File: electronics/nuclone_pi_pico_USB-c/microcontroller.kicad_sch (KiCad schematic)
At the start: 3 parts, among them J5 Conn_02x06_Odd_Even, U3 RaspberryPiPico

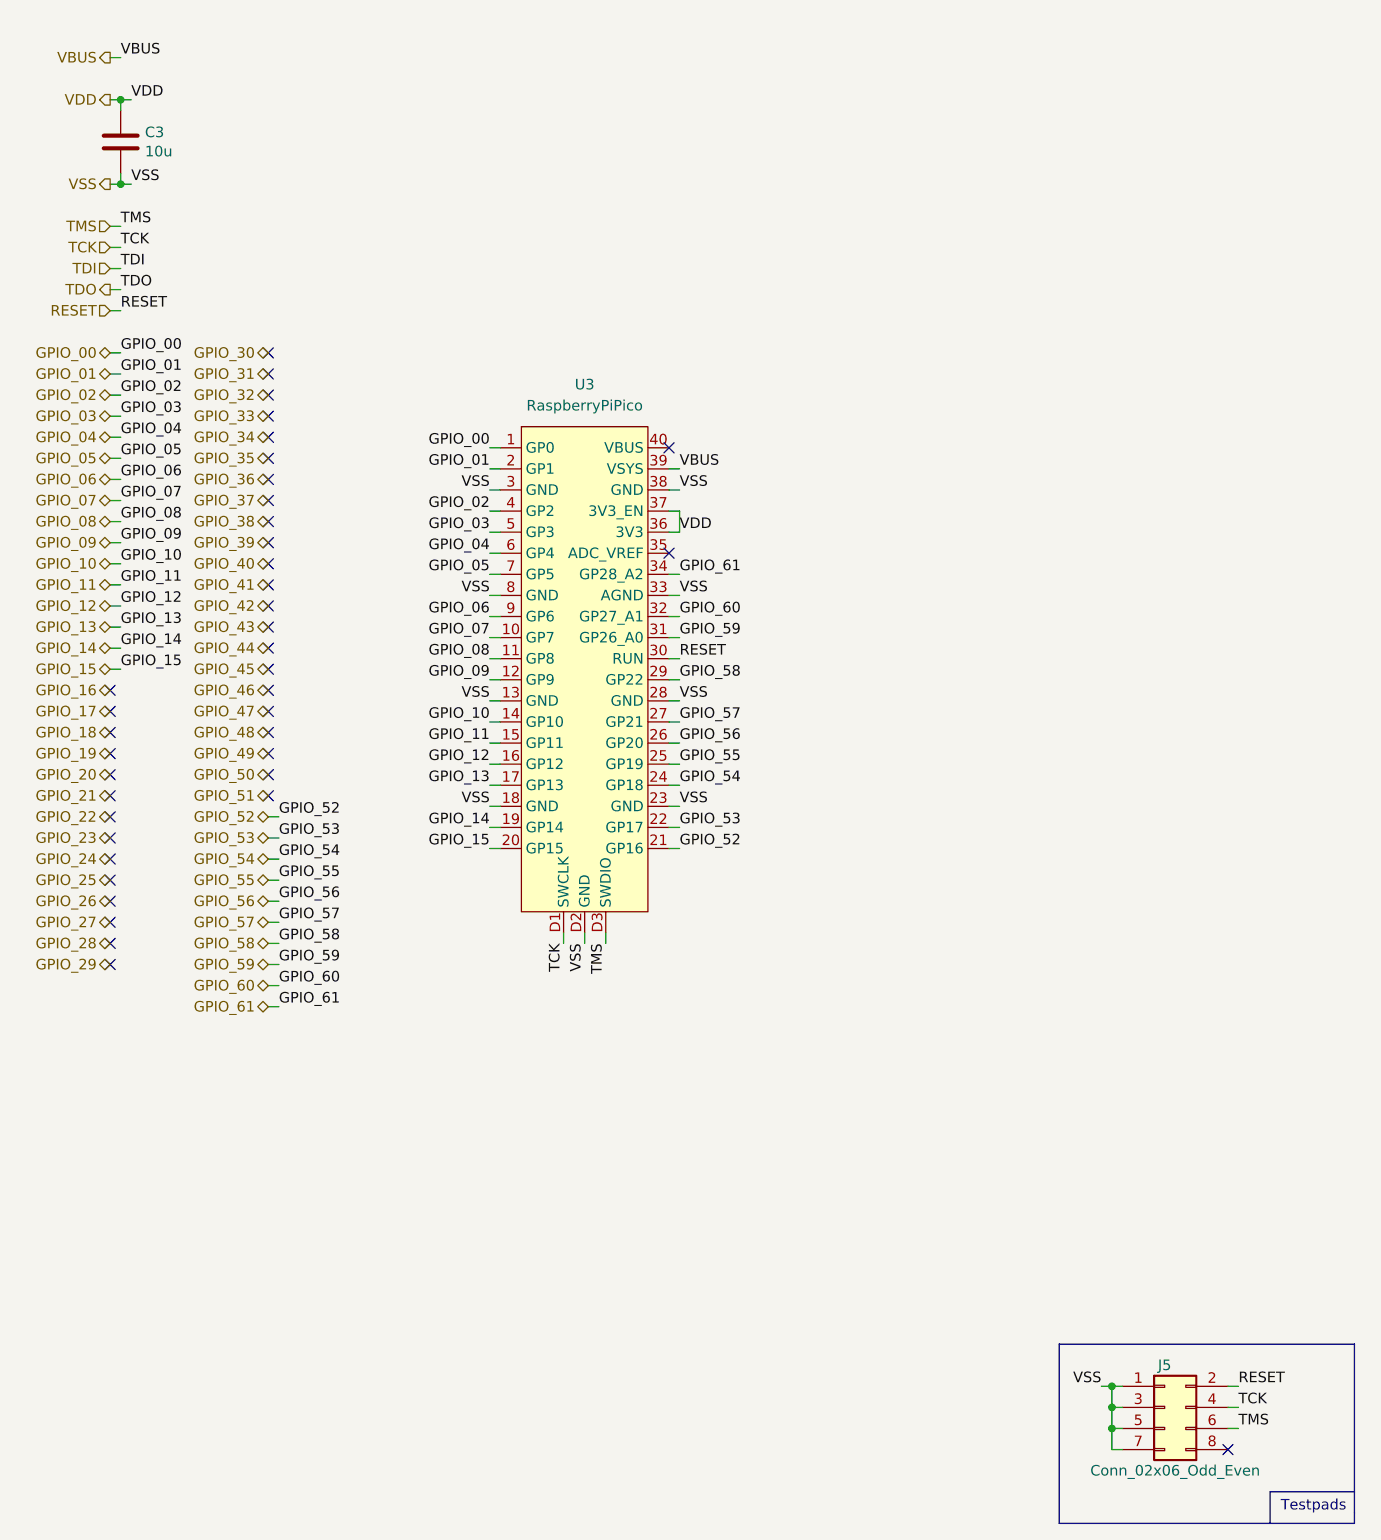
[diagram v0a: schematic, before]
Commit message: added USB-C connection, routing and placing bits and pieces
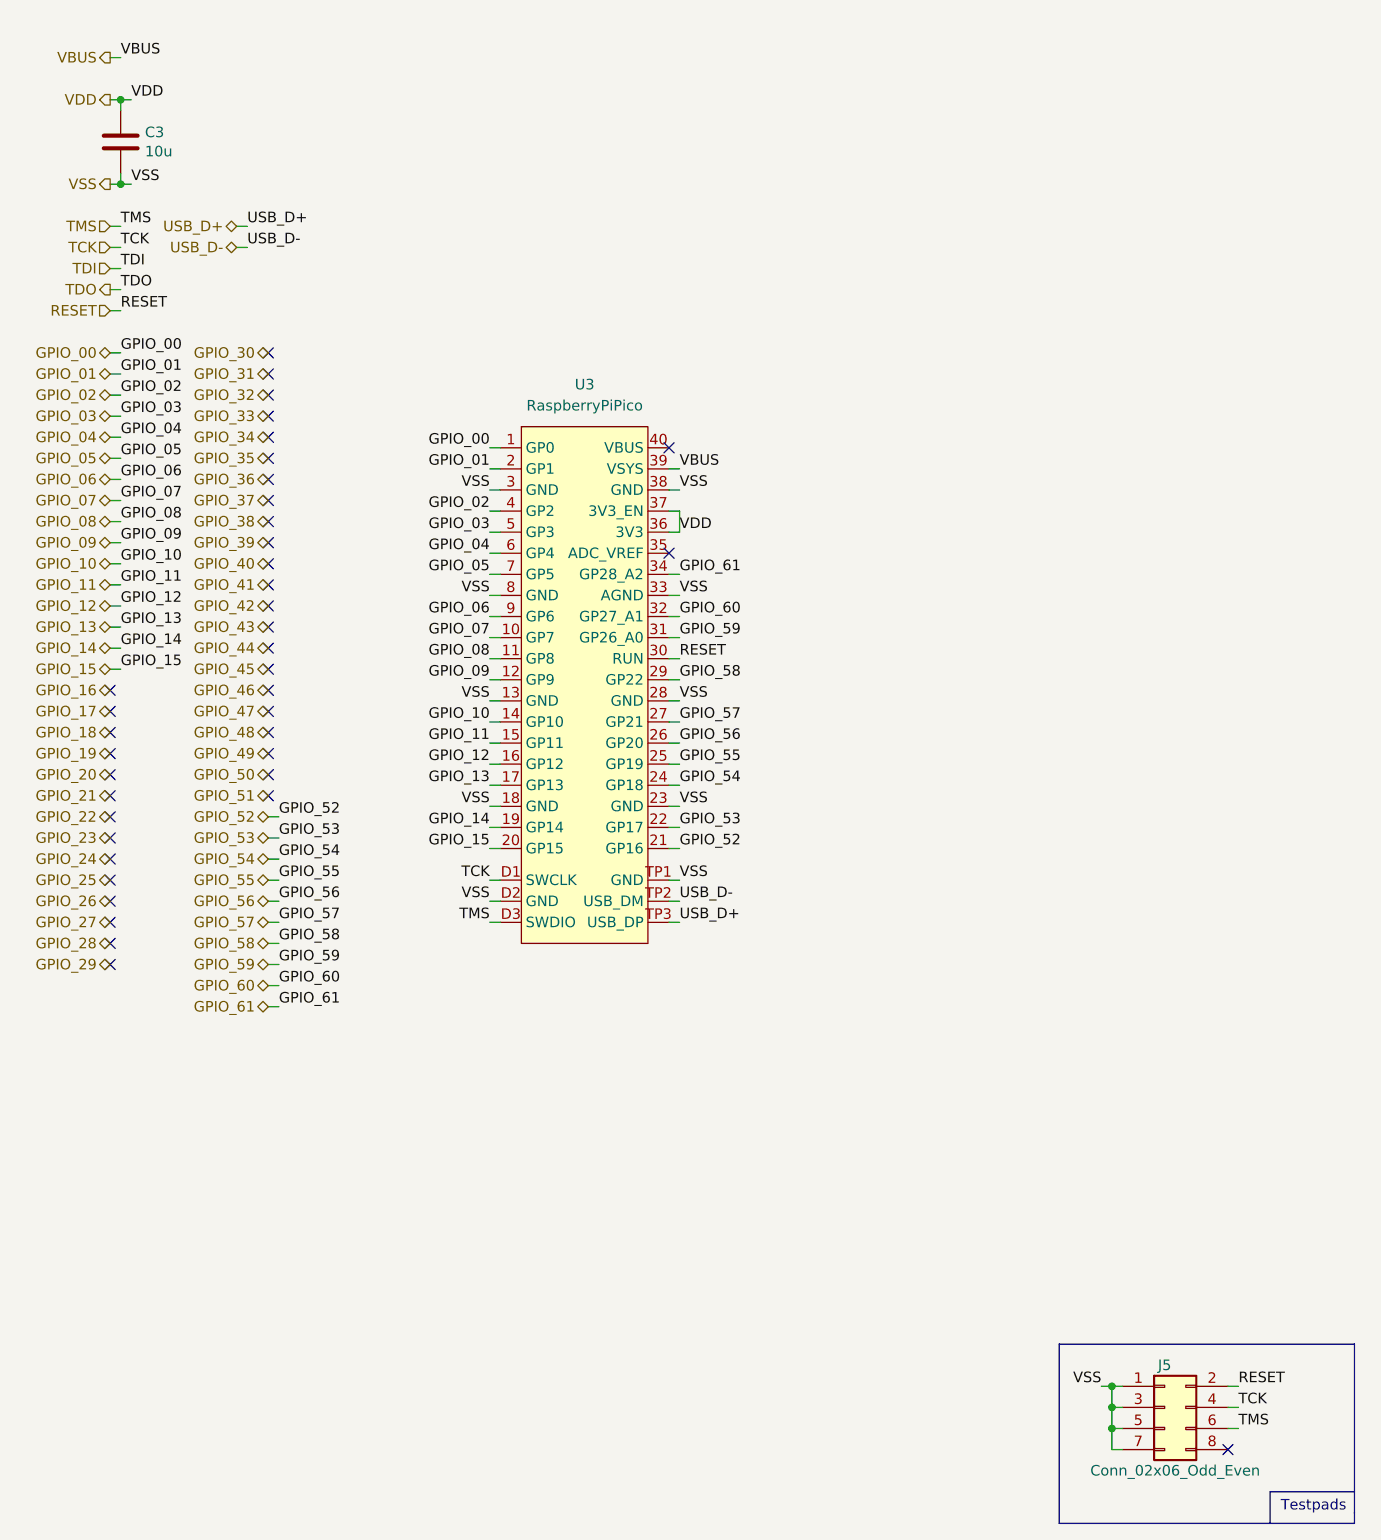
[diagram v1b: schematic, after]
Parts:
- U3: footprint Module_RaspberryPi_Pico:RaspberryPi_Pico_Original_SMD -> SquantorModules:RaspberryPi_Pico_Original_SMD_nokeepout; symbol SquantorModules:RaspberryPiPico -> SquantorModules:RaspberryPiPico_extra
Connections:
- net VSS: now also U3.TP1 (GND)
- new net USB_D+: U3.TP3 (USB_DP)
- new net USB_D-: U3.TP2 (USB_DM)
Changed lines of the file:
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@@
-    (stroke (width 0) (type default))
-  )
-  (wire (pts (xy 81.28 123.19) (xy 81.28 124.46))
     (stroke (width 0) (type default))
   )
@@
     (stroke (width 0) (type default))
   )
+  (wire (pts (xy 69.85 121.92) (xy 71.12 121.92))
+    (stroke (width 0) (type default))
+  )
   (wire (pts (xy 69.85 90.17) (xy 71.12 90.17))
     (stroke (width 0) (type default))
@@
     (stroke (width 0) (type default))
   )
+  (wire (pts (xy 39.37 38.1) (xy 40.64 38.1))
+    (stroke (width 0) (type default))
+  )
   (wire (pts (xy 24.13 53.34) (xy 25.4 53.34))
     (stroke (width 0) (type default))
   )
+  (wire (pts (xy 91.44 121.92) (xy 92.71 121.92))
+    (stroke (width 0) (type default))
+  )
   (wire (pts (xy 158.75 182.88) (xy 160.02 182.88))
     (stroke (width 0) (type default))
   )
+  (wire (pts (xy 39.37 40.64) (xy 40.64 40.64))
+    (stroke (width 0) (type default))
+  )
   (wire (pts (xy 91.44 102.87) (xy 92.71 102.87))
     (stroke (width 0) (type default))
@@
     (stroke (width 0) (type default))
   )
+  (wire (pts (xy 69.85 116.84) (xy 71.12 116.84))
+    (stroke (width 0) (type default))
+  )
   (wire (pts (xy 24.13 33.02) (xy 25.4 33.02))
     (stroke (width 0) (type default))
@@
     (stroke (width 0) (type default))
   )
-  (wire (pts (xy 78.74 123.19) (xy 78.74 124.46))
-    (stroke (width 0) (type default))
-  )
   (wire (pts (xy 43.18 124.46) (xy 44.45 124.46))
     (stroke (width 0) (type default))
@@
     (stroke (width 0) (type default))
   )
-  (wire (pts (xy 83.82 123.19) (xy 83.82 124.46))
-    (stroke (width 0) (type default))
-  )
   (wire (pts (xy 43.18 119.38) (xy 44.45 119.38))
     (stroke (width 0) (type default))
@@
     (stroke (width 0) (type default))
   )
+  (wire (pts (xy 69.85 119.38) (xy 71.12 119.38))
+    (stroke (width 0) (type default))
+  )
   (wire (pts (xy 24.13 22.86) (xy 25.4 22.86))
     (stroke (width 0) (type default))
@@
     (stroke (width 0) (type default))
   )
+  (wire (pts (xy 91.44 116.84) (xy 92.71 116.84))
+    (stroke (width 0) (type default))
+  )
   (wire (pts (xy 69.85 102.87) (xy 71.12 102.87))
     (stroke (width 0) (type default))
@@
     (stroke (width 0) (type default))
   )
+  (wire (pts (xy 91.44 119.38) (xy 92.71 119.38))
+    (stroke (width 0) (type default))
+  )
   (wire (pts (xy 91.44 110.49) (xy 92.71 110.49))
     (stroke (width 0) (type default))
@@
     (effects (font (size 1.27 1.27)) (justify left bottom))
   )
+  (label "USB_D-" (at 40.64 40.64 0) (fields_autoplaced)
+    (effects (font (size 1.27 1.27)) (justify left bottom))
+  )
   (label "GPIO_54" (at 92.71 105.41 0) (fields_autoplaced)
     (effects (font (size 1.27 1.27)) (justify left bottom))
@@
     (effects (font (size 1.27 1.27)) (justify right bottom))
   )
-  (label "TCK" (at 78.74 124.46 270) (fields_autoplaced)
+  (label "TCK" (at 69.85 116.84 180) (fields_autoplaced)
     (effects (font (size 1.27 1.27)) (justify right bottom))
   )
@@
     (effects (font (size 1.27 1.27)) (justify left bottom))
   )
-  (label "VSS" (at 81.28 124.46 270) (fields_autoplaced)
-    (effects (font (size 1.27 1.27)) (justify right bottom))
+  (label "VSS" (at 69.85 119.38 180) (fields_autoplaced)
+    (effects (font (size 1.27 1.27)) (justify right bottom))
+  )
+  (label "USB_D+" (at 92.71 121.92 0) (fields_autoplaced)
+    (effects (font (size 1.27 1.27)) (justify left bottom))
   )
   (label "GPIO_57" (at 44.45 121.92 0) (fields_autoplaced)
@@
     (effects (font (size 1.27 1.27)) (justify left bottom))
   )
-  (label "TMS" (at 83.82 124.46 270) (fields_autoplaced)
+  (label "TMS" (at 69.85 121.92 180) (fields_autoplaced)
     (effects (font (size 1.27 1.27)) (justify right bottom))
   )
@@
     (effects (font (size 1.27 1.27)) (justify left bottom))
   )
+  (label "USB_D-" (at 92.71 119.38 0) (fields_autoplaced)
+    (effects (font (size 1.27 1.27)) (justify left bottom))
+  )
   (label "TDI" (at 25.4 43.18 0) (fields_autoplaced)
     (effects (font (size 1.27 1.27)) (justify left bottom))
@@
     (effects (font (size 1.27 1.27)) (justify right bottom))
   )
+  (label "USB_D+" (at 40.64 38.1 0) (fields_autoplaced)
+    (effects (font (size 1.27 1.27)) (justify left bottom))
+  )
   (label "GPIO_53" (at 92.71 110.49 0) (fields_autoplaced)
     (effects (font (size 1.27 1.27)) (justify left bottom))
   )
+  (label "VSS" (at 92.71 116.84 0) (fields_autoplaced)
+    (effects (font (size 1.27 1.27)) (justify left bottom))
+  )
   (label "TMS" (at 160.02 182.88 0) (fields_autoplaced)
     (effects (font (size 1.27 1.27)) (justify left bottom))
@@
     (effects (font (size 1.27 1.27)) (justify right))
   )
+  (hierarchical_label "USB_D+" (shape bidirectional) (at 39.37 38.1 180) (fields_autoplaced)
+    (effects (font (size 1.27 1.27)) (justify right))
+  )
   (hierarchical_label "GPIO_61" (shape bidirectional) (at 43.18 132.08 180) (fields_autoplaced)
     (effects (font (size 1.27 1.27)) (justify right))
@@
   )
   (hierarchical_label "GPIO_04" (shape bidirectional) (at 24.13 63.5 180) (fields_autoplaced)
+    (effects (font (size 1.27 1.27)) (justify right))
+  )
+  (hierarchical_label "USB_D-" (shape bidirectional) (at 39.37 40.64 180) (fields_autoplaced)
     (effects (font (size 1.27 1.27)) (justify right))
   )
@@
     (pin "2")
     (instances
-      (project "nuclone_pi_pico_direct"
+      (project "nuclone_pi_pico_USB-c"
         (path "/f714ce77-1b03-46de-8ce2-42d10401024e/00000000-0000-0000-0000-00006127a958"
           (reference "C3") (unit 1)
@@
         )
       )
-      (project "nuclone_pi_pico_direct"
+      (project "nuclone_pi_pico_USB-c"
         (path "/f714ce77-1b03-46de-8ce2-42d10401024e/00000000-0000-0000-0000-00006127a958"
           (reference "J5") (unit 1)
@@
     )
   )
-  (symbol (lib_id "SquantorModules:RaspberryPiPico") (at 81.28 88.9 0) (unit 1)
+  (symbol (lib_id "SquantorModules:RaspberryPiPico_extra") (at 81.28 88.9 0) (unit 1)
     (in_bom yes) (on_board yes) (dnp no) (fields_autoplaced)
     (property "Reference" "U3" (at 81.28 57.15 0)
@@
       (effects (font (size 1.27 1.27)))
     )
-    (property "Footprint" "Module_RaspberryPi_Pico:RaspberryPi_Pico_Original_SMD" (at 81.28 88.9 0)
+    (property "Footprint" "SquantorModules:RaspberryPi_Pico_Original_SMD_nokeepout" (at 81.28 88.9 0)
       (effects (font (size 1.27 1.27)) hide)
     )
@@
     (pin "15")
     (pin "14")
+    (pin "TP1")
+    (pin "TP3")
+    (pin "TP2")
     (instances
-      (project "nuclone_pi_pico_direct"
+      (project "nuclone_pi_pico_USB-c"
         (path "/f714ce77-1b03-46de-8ce2-42d10401024e/00000000-0000-0000-0000-00006127a958"
           (reference "U3") (unit 1)

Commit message: moved pico down more, changed routing
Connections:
- net VBUS: now also U3.40 (VBUS); no longer U3.39 (VSYS)
- new net VSYS: U3.39 (VSYS)
- no-connect marks 39 -> 38
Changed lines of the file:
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@@
   (no_connect (at 158.75 185.42))
   (no_connect (at 24.13 99.06))
-  (no_connect (at 91.44 64.77))
   (no_connect (at 43.18 78.74))
   (wire (pts (xy 91.44 113.03) (xy 92.71 113.03))
@@
     (stroke (width 0) (type default))
   )
+  (wire (pts (xy 24.13 15.24) (xy 25.4 15.24))
+    (stroke (width 0) (type default))
+  )
   (wire (pts (xy 24.13 91.44) (xy 25.4 91.44))
     (stroke (width 0) (type default))
@@
     (stroke (width 0) (type default))
   )
+  (wire (pts (xy 91.44 64.77) (xy 92.71 64.77))
+    (stroke (width 0) (type default))
+  )
   (wire (pts (xy 24.13 76.2) (xy 25.4 76.2))
     (stroke (width 0) (type default))
@@
     (effects (font (size 1.27 1.27)) (justify left bottom))
   )
-  (label "VBUS" (at 92.71 67.31 0) (fields_autoplaced)
+  (label "VBUS" (at 92.71 64.77 0) (fields_autoplaced)
     (effects (font (size 1.27 1.27)) (justify left bottom))
   )
@@
     (effects (font (size 1.27 1.27)) (justify left bottom))
   )
+  (label "VSYS" (at 92.71 67.31 0) (fields_autoplaced)
+    (effects (font (size 1.27 1.27)) (justify left bottom))
+  )
   (label "GPIO_52" (at 44.45 109.22 0) (fields_autoplaced)
     (effects (font (size 1.27 1.27)) (justify left bottom))
@@
     (effects (font (size 1.27 1.27)) (justify right bottom))
   )
+  (label "VSYS" (at 25.4 15.24 0) (fields_autoplaced)
+    (effects (font (size 1.27 1.27)) (justify left bottom))
+  )
   (label "RESET" (at 92.71 90.17 0) (fields_autoplaced)
     (effects (font (size 1.27 1.27)) (justify left bottom))
@@
     (effects (font (size 1.27 1.27)) (justify right bottom))
   )
+  (hierarchical_label "VSYS" (shape output) (at 24.13 15.24 180) (fields_autoplaced)
+    (effects (font (size 1.27 1.27)) (justify right))
+  )
   (hierarchical_label "GPIO_30" (shape bidirectional) (at 43.18 53.34 180) (fields_autoplaced)
     (effects (font (size 1.27 1.27)) (justify right))
@@
     (effects (font (size 1.27 1.27)) (justify right))
   )
-  (hierarchical_label "VBUS" (shape output) (at 24.13 17.78 180) (fields_autoplaced)
-    (effects (font (size 1.27 1.27)) (justify right))
-  )
+  (hierarchical_label "VBUS" (shape input) (at 24.13 17.78 180) (fields_autoplaced)
+    (effects (font (size 1.27 1.27)) (justify right))
+  )

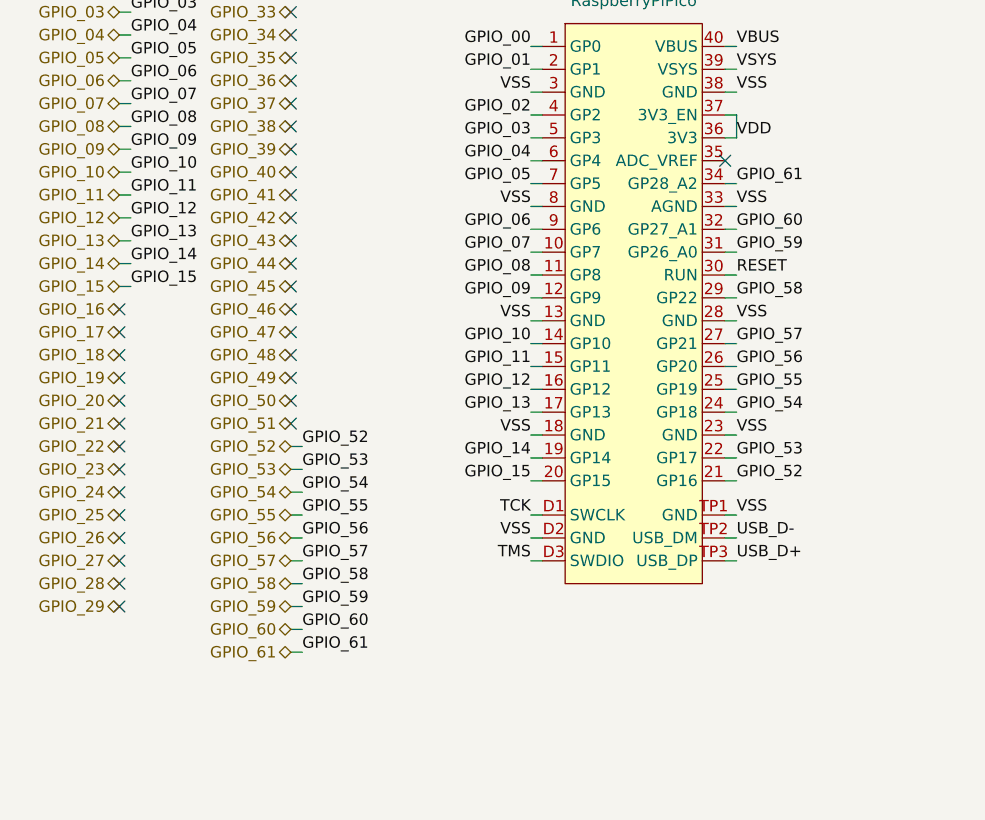
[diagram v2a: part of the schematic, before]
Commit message: changing pinouts to match RP2040 nuclone
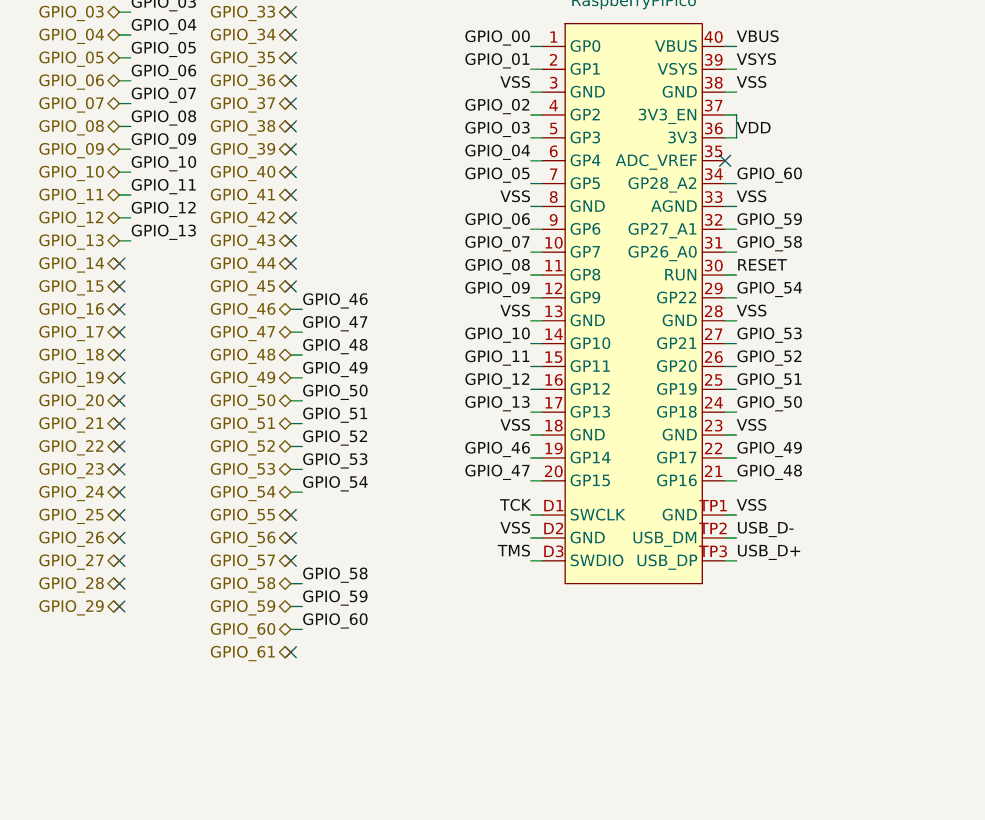
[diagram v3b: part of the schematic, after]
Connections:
- net GPIO_14: no longer U3.19 (GP14)
- net GPIO_15: no longer U3.20 (GP15)
- net GPIO_46: now also U3.19 (GP14)
- net GPIO_47: now also U3.20 (GP15)
- net GPIO_48: now also U3.21 (GP16)
- net GPIO_49: now also U3.22 (GP17)
- net GPIO_50: now also U3.24 (GP18)
- net GPIO_51: now also U3.25 (GP19)
- net GPIO_52: now also U3.26 (GP20); no longer U3.21 (GP16)
- net GPIO_53: now also U3.27 (GP21); no longer U3.22 (GP17)
- net GPIO_54: now also U3.29 (GP22); no longer U3.24 (GP18)
- net GPIO_55: no longer U3.25 (GP19)
- net GPIO_56: no longer U3.26 (GP20)
- net GPIO_57: no longer U3.27 (GP21)
- net GPIO_58: now also U3.31 (GP26_A0); no longer U3.29 (GP22)
- net GPIO_59: now also U3.32 (GP27_A1); no longer U3.31 (GP26_A0)
- net GPIO_60: now also U3.34 (GP28_A2); no longer U3.32 (GP27_A1)
- net GPIO_61: no longer U3.34 (GP28_A2)
